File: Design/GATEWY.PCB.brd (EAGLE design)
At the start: 81.7 x 51.7 mm, 29 parts, among them IC1 FT232RL, SW1 SWITCH-TACTILE, SW2 RA_BUTTON, U1 WS2801, X1 USBPTH

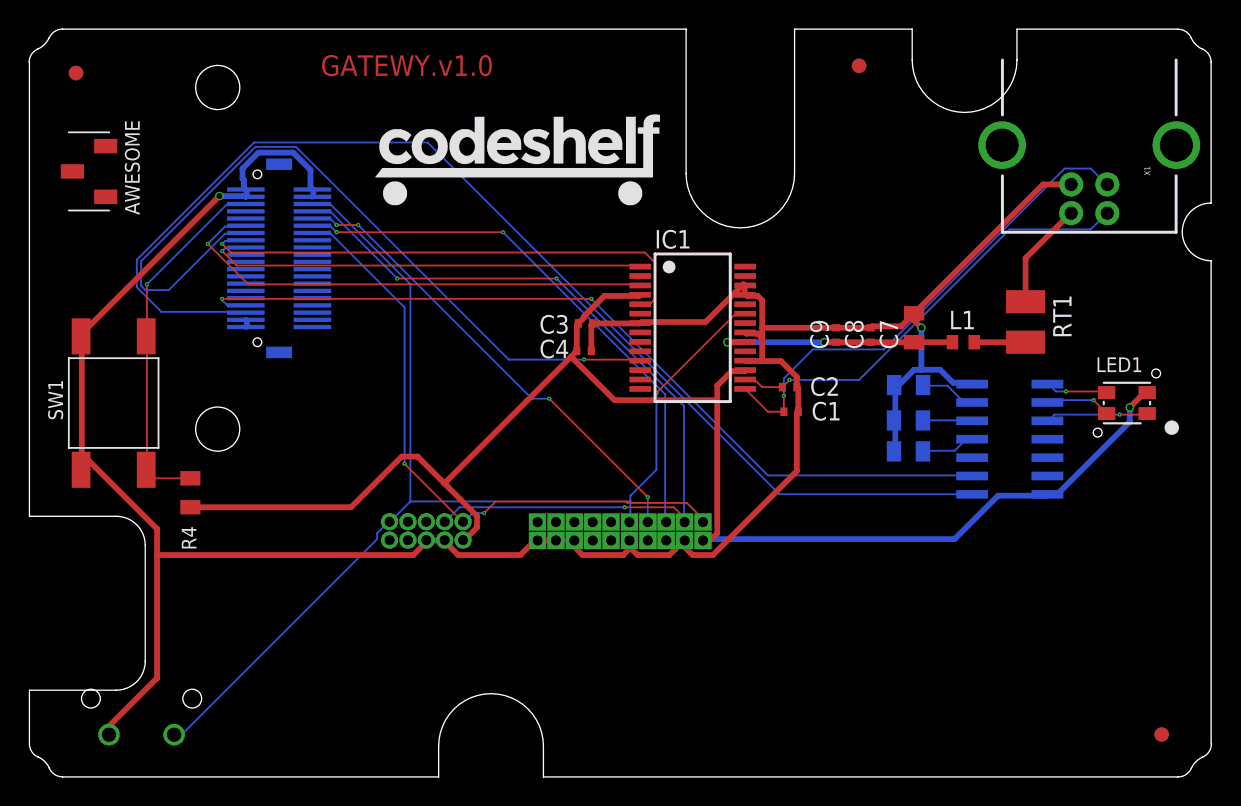
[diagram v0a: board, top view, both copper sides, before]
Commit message: Use the new Codeshelf DRU file to generate and test the board.
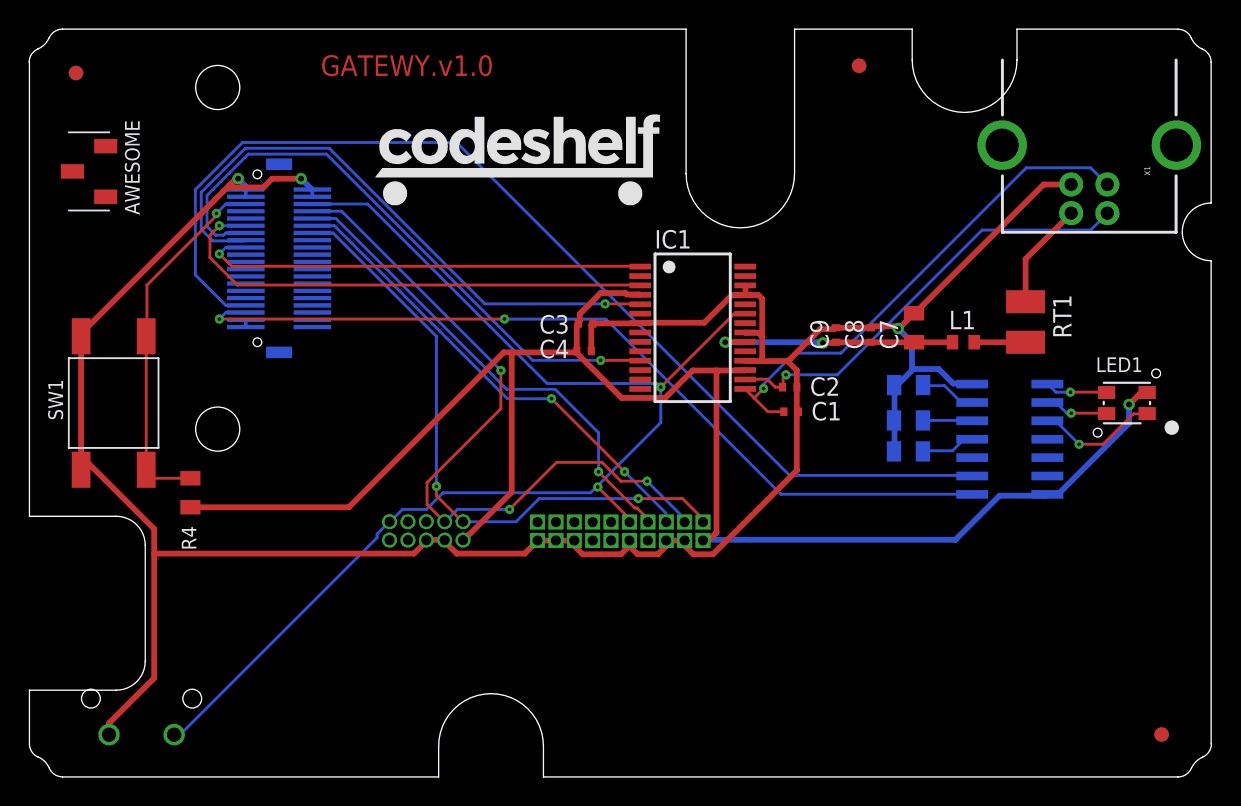
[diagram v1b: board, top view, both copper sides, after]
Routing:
- net N$14: track 81.3 -> 59.0 mm, vias 0 -> 2
- net N$10: track 58.8 -> 74.8 mm, vias 2 -> 0
- net N$3: track 54.6 -> 42.2 mm
- net +3V3: track 105.8 -> 114.9 mm
- net N$9: track 35.9 -> 42.0 mm
- net N$18: track 56.9 -> 50.8 mm
- net SW2: track 80.6 -> 85.8 mm, vias 1 -> 2
- net GND: track 182.9 -> 178.1 mm, vias 2 -> 3
- net N$8: track 38.1 -> 33.3 mm
- net N$7: track 7.14 -> 8.45 mm
- net N$20: track 32.9 -> 33.6 mm, vias 4 -> 1
- net N$2: track 34.2 -> 34.8 mm
- net USB+: track 34.4 -> 35.0 mm

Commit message: Change the JTAG header to SMT
Also remove the SWD header.
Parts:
- removed SWD: (no value), KW2:2X5HDR
- JTAG: value 2X10JTAG -> 2X10JTAGSMD; device KW2:2X10JTAG -> KW2:2X10JTAG-SMD
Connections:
- net +3V3: no longer SWD.P$1
- net GND: no longer SWD.P$3, SWD.P$5
- net N$18: no longer SWD.P$4
- net N$6: no longer SWD.P$2
- net SW2: no longer SWD.P$10
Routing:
- net N$14: track 59.0 -> 80.5 mm, vias 2 -> 0
- net N$18: track 50.8 -> 34.1 mm, vias 3 -> 0
- net N$10: track 74.8 -> 58.8 mm, vias 0 -> 2
- net USB-: track 30.6 -> 41.2 mm, vias 1 -> 0
- net +3V3: track 114.9 -> 105.9 mm, vias 1 -> 2
- net N$6: track 43.1 -> 34.5 mm
- net GND: track 178.1 -> 182.4 mm, vias 3 -> 4
- net N$2: track 34.8 -> 39.0 mm
- net SW2: track 85.8 -> 84.0 mm
- net USB+: track 35.0 -> 36.3 mm, vias 1 -> 0
- net N$20: track 33.6 -> 32.3 mm, vias 1 -> 2
- net N$3: track 42.2 -> 43.2 mm
- net N$15: track 31.5 -> 32.4 mm
- net N$9: track 42.0 -> 43.0 mm
- net N$8: track 33.3 -> 32.4 mm, vias 2 -> 0

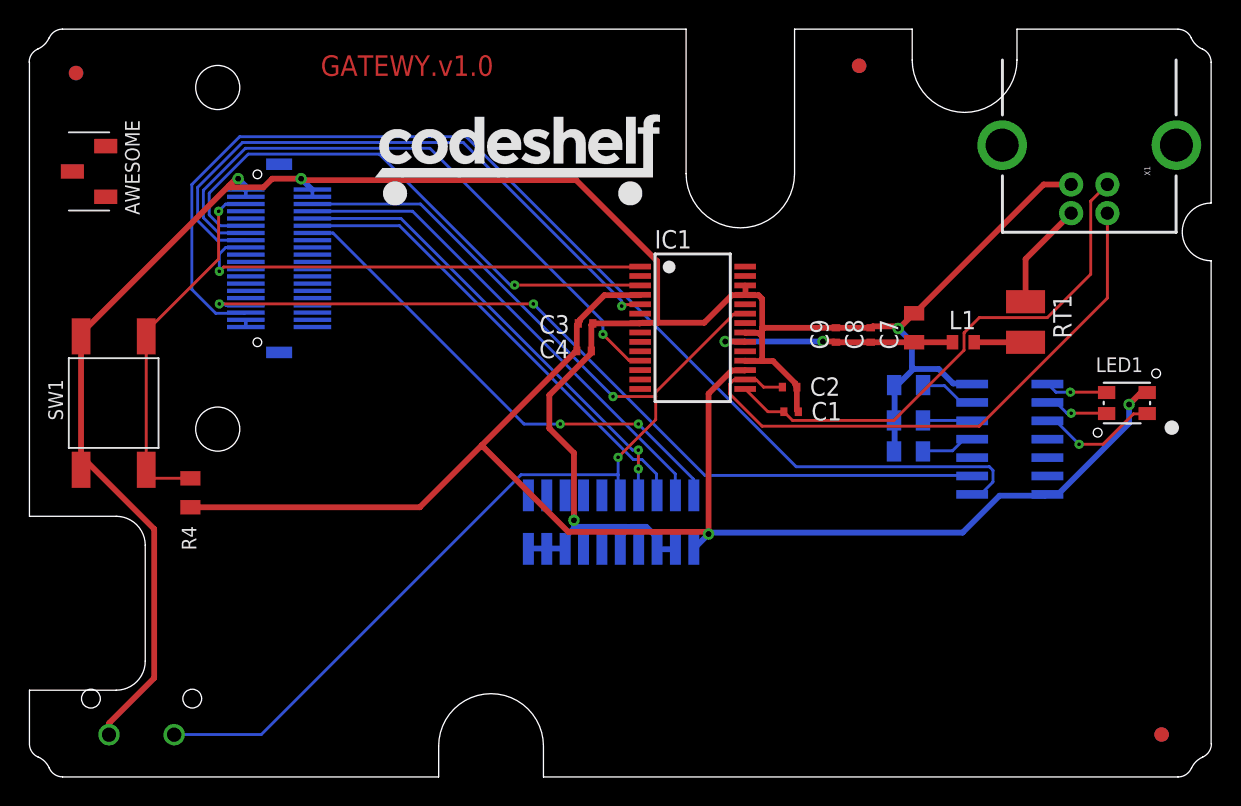
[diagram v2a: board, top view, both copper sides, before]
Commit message: Redo the board with larger vias (from the new CS "std" DRU file.
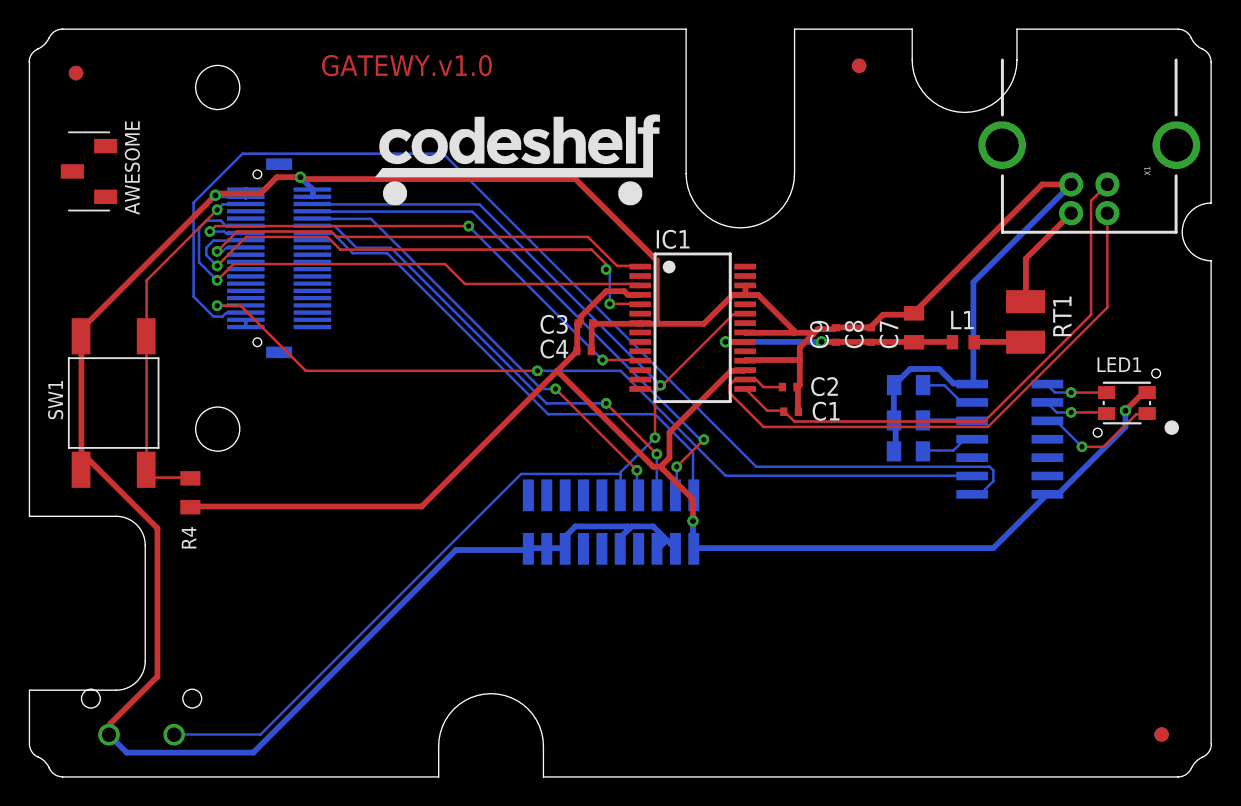
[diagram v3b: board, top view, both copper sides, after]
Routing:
- net GND: track 182.4 -> 222.0 mm, vias 4 -> 2
- net N$3: track 43.2 -> 36.3 mm, vias 1 -> 3
- net N$9: track 43.0 -> 37.9 mm, vias 1 -> 3
- net +3V3: track 105.9 -> 101.2 mm
- net N$18: track 34.1 -> 38.2 mm, vias 0 -> 2
- net N$14: track 80.5 -> 79.1 mm
- net N$6: track 34.5 -> 35.6 mm, vias 2 -> 0
- net USB+: track 36.3 -> 37.4 mm
- net N$2: track 39.0 -> 38.0 mm
- net N$20: track 32.3 -> 31.4 mm
- net N$8: track 32.4 -> 33.2 mm, vias 0 -> 2

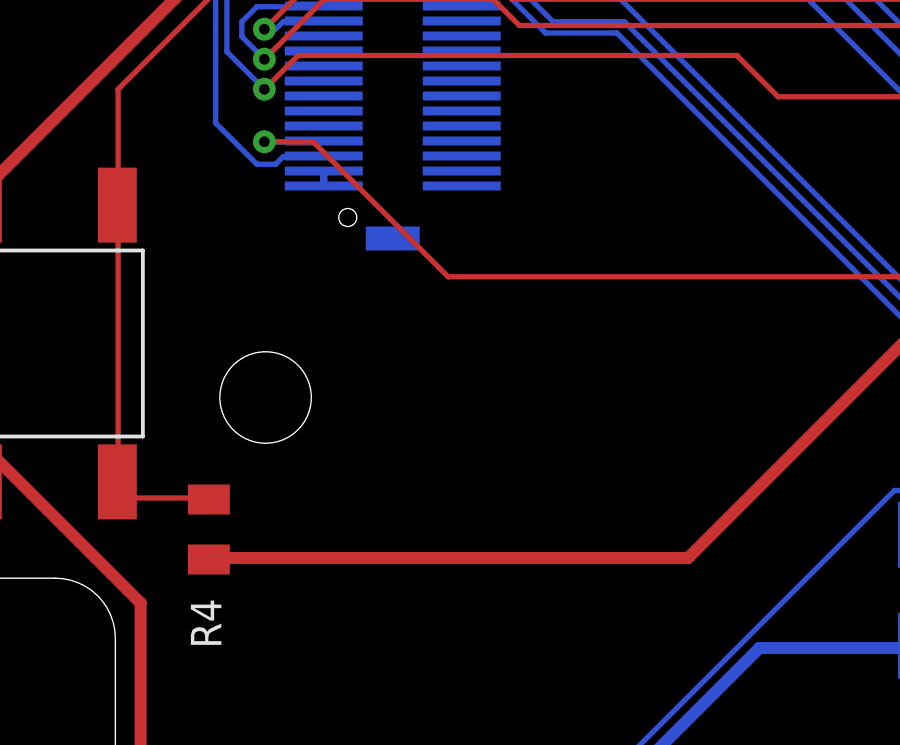
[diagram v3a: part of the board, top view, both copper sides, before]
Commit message: Fix a problem with 3.3V
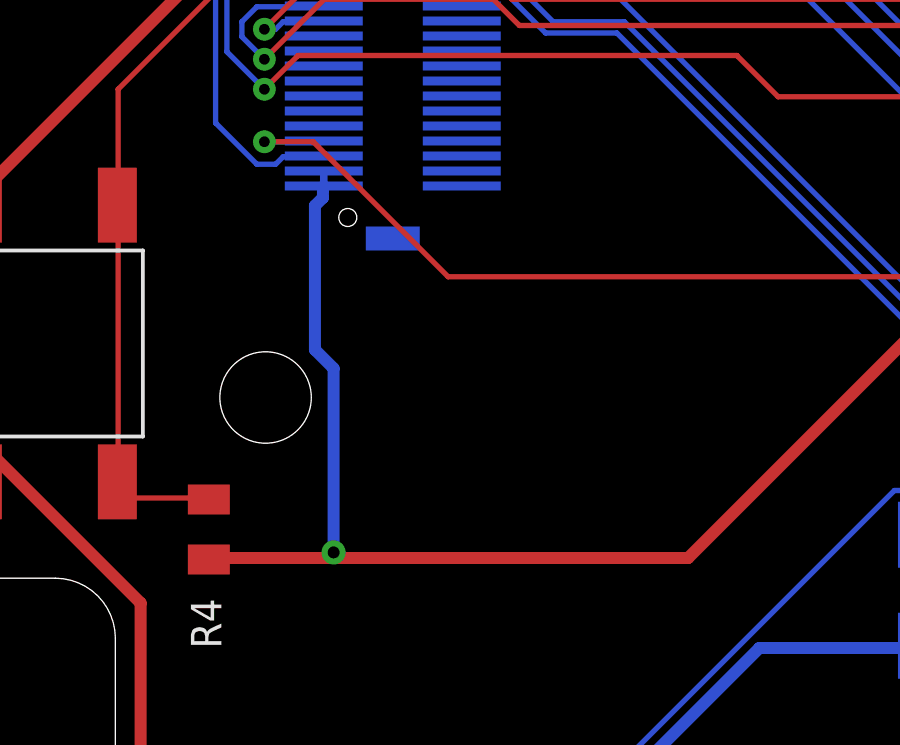
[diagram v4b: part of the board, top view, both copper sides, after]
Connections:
- net N$18 renamed JTAG_CLK
- net N$20 renamed JTAG_TDI
- net N$6 renamed JTAG_TMS
- net N$8 renamed JTAG_TDO
- net SW2 renamed RESET
- removed net N$1: KW2.P$37, KW2.P$39
- net +3V3: now also KW2.P$37, KW2.P$39
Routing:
- net +3V3: track 101.2 -> 114.5 mm, vias 2 -> 3
- net N$1: track 0.50 -> 0.00 mm
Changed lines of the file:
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@@
 <wire x1="38.375" y1="31.5" x2="38.2" y2="31.4" width="0.4" layer="1"/>
 <wire x1="42.375" y1="33.375" x2="42.475" y2="33.375" width="0.4" layer="1"/>
-<wire x1="27.375" y1="18.75" x2="11.5" y2="18.75" width="0.4" layer="1"/>
+<wire x1="27.375" y1="18.75" x2="15.5575" y2="18.75" width="0.4" layer="1"/>
+<wire x1="15.5575" y1="18.75" x2="11.5" y2="18.75" width="0.4" layer="1"/>
 <wire x1="38" y1="29.375" x2="36.75" y2="28.125" width="0.4" layer="1"/>
 <wire x1="36.75" y1="28.125" x2="27.375" y2="18.75" width="0.4" layer="1"/>
@@
 <via x="76" y="25.375" extent="1-16" drill="0.4"/>
 <via x="46.125" y="17.75" extent="1-16" drill="0.4"/>
+<contactref element="KW2" pad="P$37"/>
+<contactref element="KW2" pad="P$39"/>
+<wire x1="15.23" y1="31.65" x2="15.23" y2="31.15" width="0.254" layer="16"/>
+<wire x1="15.2019" y1="30.7594" x2="15.2019" y2="31.0261" width="0.4" layer="16"/>
+<wire x1="14.9352" y1="30.4927" x2="15.2019" y2="30.7594" width="0.4" layer="16"/>
+<wire x1="14.9352" y1="25.6921" x2="14.9352" y2="30.4927" width="0.4" layer="16"/>
+<wire x1="15.5575" y1="25.0698" x2="14.9352" y2="25.6921" width="0.4" layer="16"/>
+<wire x1="15.5575" y1="18.9357" x2="15.5575" y2="25.0698" width="0.4" layer="16"/>
+<wire x1="15.2019" y1="31.0261" x2="15.23" y2="31.15" width="0.4" layer="16"/>
+<wire x1="15.5575" y1="18.9357" x2="15.5575" y2="18.75" width="0.4" layer="1"/>
+<via x="15.5575" y="18.9357" extent="1-16" drill="0.4"/>
 </signal>
 <signal name="N$4">
@@
 <wire x1="15.125" y1="32.125" x2="15.23" y2="32.15" width="0.1778" layer="16"/>
 </signal>
-<signal name="N$18">
+<signal name="JTAG_CLK">
 <contactref element="KW2" pad="P$8"/>
 <contactref element="JTAG" pad="P$4"/>
@@
 <via x="46.875" y="23.375" extent="1-16" drill="0.3556"/>
 </signal>
-<signal name="N$20">
+<signal name="JTAG_TDI">
 <contactref element="KW2" pad="P$10"/>
 <contactref element="JTAG" pad="P$8"/>
@@
 <via x="36.625" y="26.875" extent="1-16" drill="0.3556"/>
 </signal>
-<signal name="N$6">
+<signal name="JTAG_TMS">
 <contactref element="KW2" pad="P$14"/>
 <contactref element="JTAG" pad="P$2"/>
@@
 <wire x1="19.875" y1="37.625" x2="19.83" y2="37.65" width="0.1778" layer="16"/>
 </signal>
-<signal name="N$8">
+<signal name="JTAG_TDO">
 <contactref element="KW2" pad="P$12"/>
 <contactref element="JTAG" pad="P$6"/>
@@
 <via x="40.125" y="25.875" extent="1-16" drill="0.3556"/>
 </signal>
-<signal name="SW2">
+<signal name="RESET">
 <contactref element="KW2" pad="P$6"/>
 <contactref element="JTAG" pad="P$10"/>
@@
 <wire x1="69" y1="30.125" x2="69.1" y2="30.1" width="0.4" layer="1"/>
 </signal>
-<signal name="N$1" class="1">
-<contactref element="KW2" pad="P$37"/>
-<contactref element="KW2" pad="P$39"/>
-<wire x1="15.23" y1="31.65" x2="15.23" y2="31.15" width="0.254" layer="16"/>
-</signal>
 <signal name="N$2">

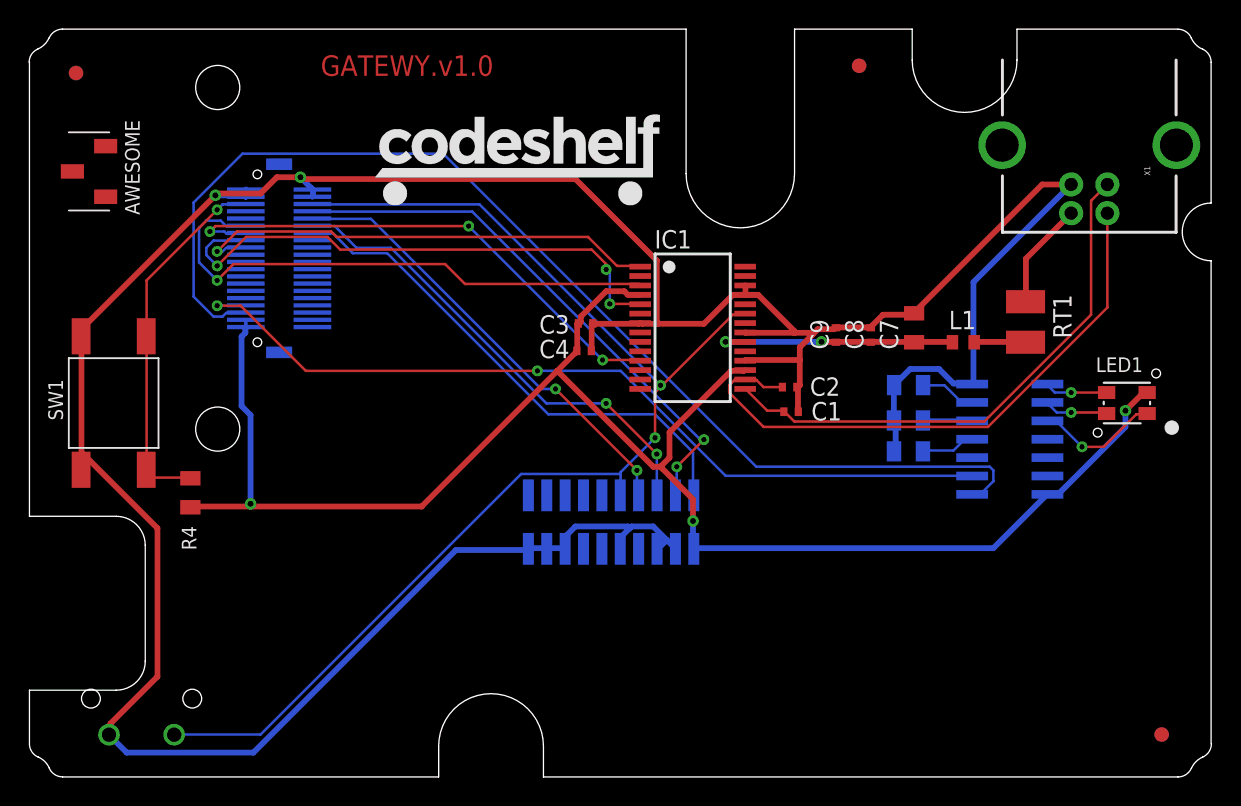
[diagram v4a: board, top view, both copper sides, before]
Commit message: Fix the FTDI UART pins.
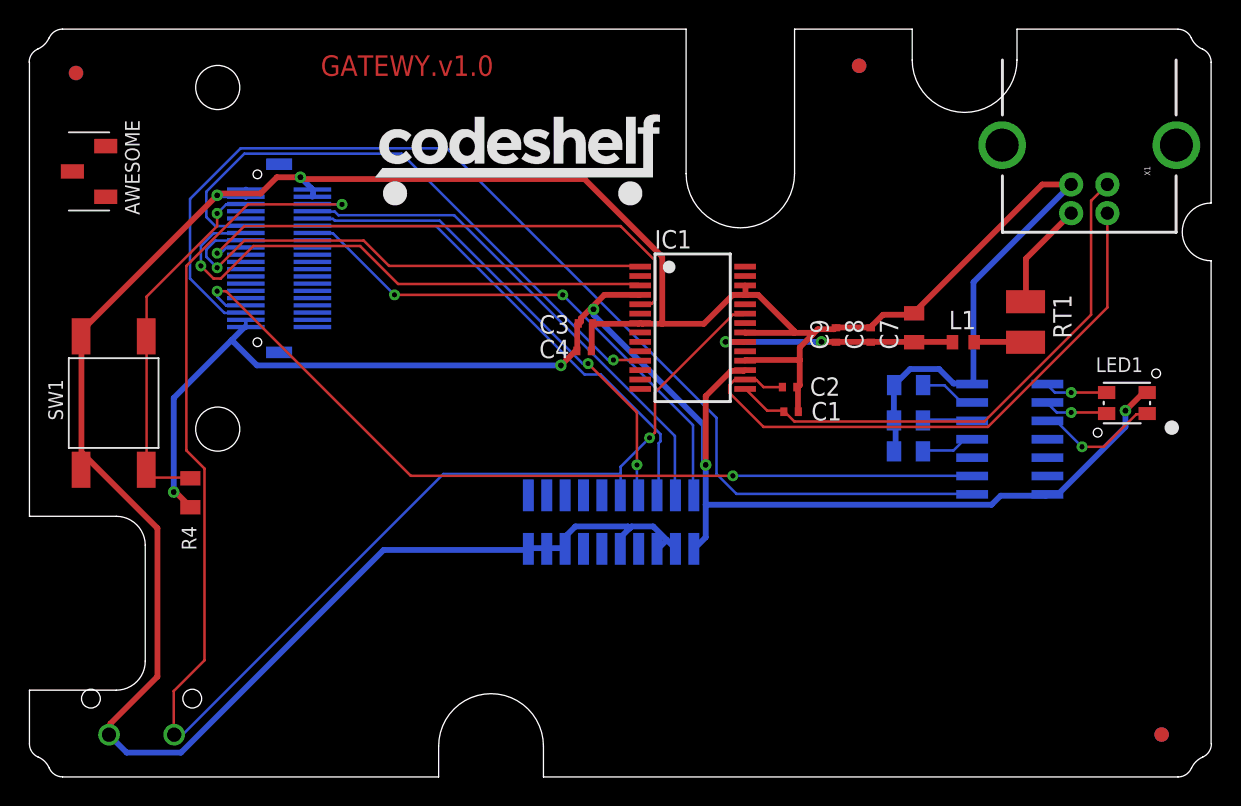
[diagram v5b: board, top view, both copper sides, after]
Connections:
- removed net N$15: IC1.1, KW2.P$17
- removed net N$2: IC1.3, KW2.P$11
- removed net N$3: IC1.11, KW2.P$13
- removed net N$9: IC1.5, KW2.P$15
- new net CTS: IC1.3, KW2.P$13
- new net RTS: IC1.11, KW2.P$11
- new net RX: IC1.1, KW2.P$15
- new net TX: IC1.5, KW2.P$17
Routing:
- net RTS: track 0.00 -> 41.7 mm, vias 0 -> 1
- net N$2: track 38.0 -> 0.00 mm, vias 1 -> 0
- net TX: track 0.00 -> 38.0 mm, vias 0 -> 1
- net N$9: track 37.9 -> 0.00 mm, vias 3 -> 0
- net CTS: track 0.00 -> 37.6 mm, vias 0 -> 1
- net N$3: track 36.3 -> 0.00 mm, vias 3 -> 0
- net RX: track 0.00 -> 35.3 mm, vias 0 -> 1
- net N$15: track 32.9 -> 0.00 mm, vias 1 -> 0
- net RESET: track 84.2 -> 103.2 mm
- net +3V3: track 114.5 -> 110.7 mm, vias 3 -> 5
- net JTAG_CLK: track 38.2 -> 35.6 mm, vias 2 -> 0
- net JTAG_TDI: track 31.4 -> 33.7 mm
- net JTAG_TDO: track 33.2 -> 34.3 mm, vias 2 -> 0
- net JTAG_TMS: track 35.6 -> 36.7 mm, vias 0 -> 2
- net N$14: track 79.1 -> 78.0 mm
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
